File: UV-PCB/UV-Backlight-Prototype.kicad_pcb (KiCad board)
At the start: 2 copper layers, 100 x 100 mm, 67 parts, among them J1 Conn_02x08_Odd_Even

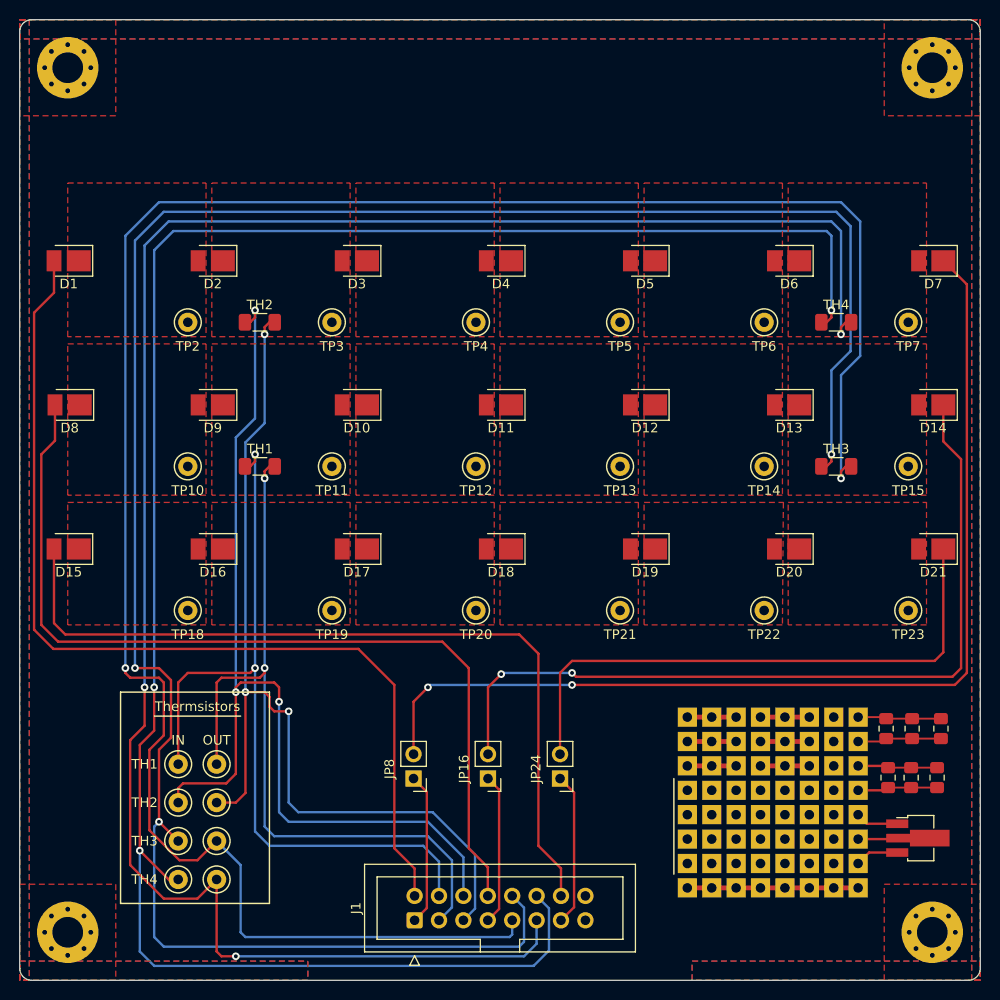
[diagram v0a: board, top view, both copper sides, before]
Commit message: UV Backlight and PS
Power Supply creation
V2 for backlight, removed thermsistors
Changed the connector, simplified the board
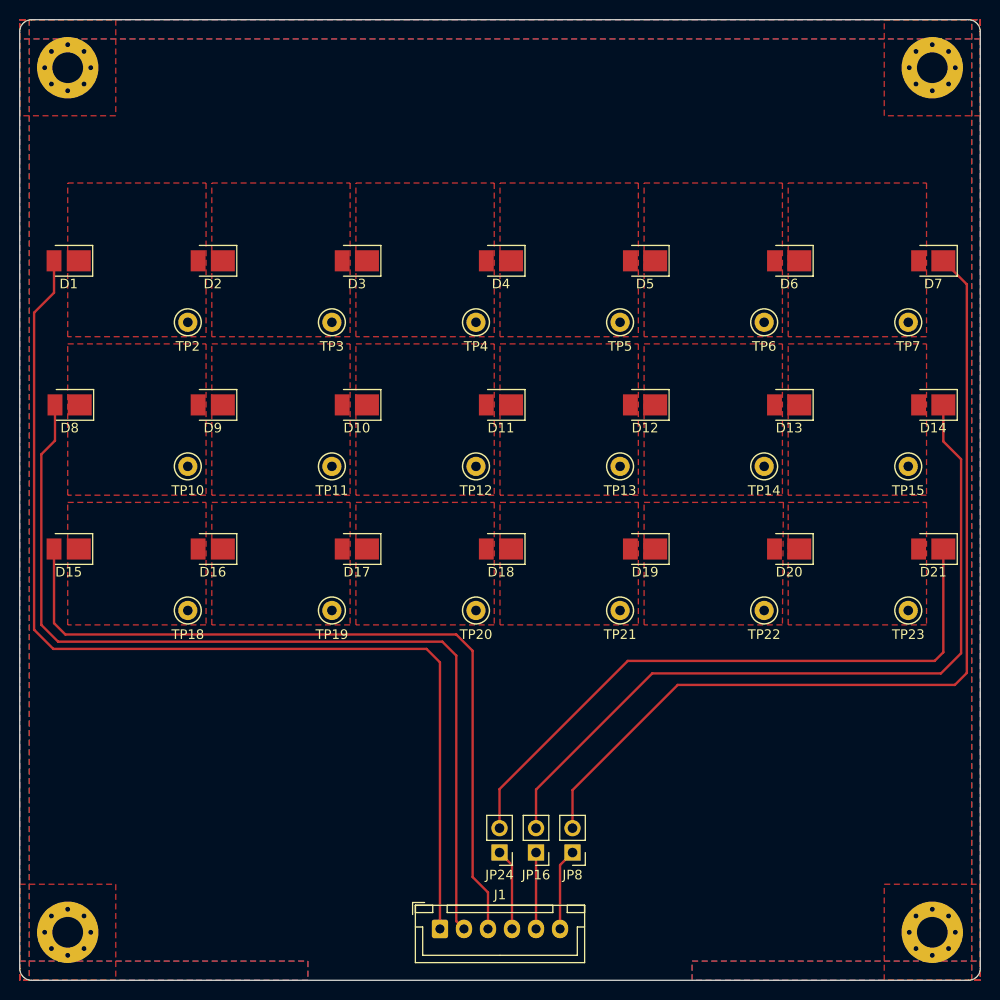
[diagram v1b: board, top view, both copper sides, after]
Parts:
- removed ?: , clipboard:e0d5eb0a-6c50-48e5-8d74-95606411ad53
- removed REF** (x6): C_0805_2012Metric_Pad1.18x1.45mm_HandSolder, Capacitor_SMD:C_0805_2012Metric_Pad1.18x1.45mm_HandSolder
- removed REF**: SOT-89-3_Handsoldering, Package_TO_SOT_SMD:SOT-89-3_Handsoldering
- removed TH1, TH2, TH3, TH4: 10K, Resistor_SMD:R_1206_3216Metric_Pad1.30x1.75mm_HandSolder
- removed TP25: T1-In, TestPoint:TestPoint_Keystone_5000-5004_Miniature
- removed TP26: T1-Out, TestPoint:TestPoint_Keystone_5000-5004_Miniature
- removed TP27: T3-In, TestPoint:TestPoint_Keystone_5000-5004_Miniature
- removed TP28: T3-Out, TestPoint:TestPoint_Keystone_5000-5004_Miniature
- removed TP29: T2-In, TestPoint:TestPoint_Keystone_5000-5004_Miniature
- removed TP30: T2-Out, TestPoint:TestPoint_Keystone_5000-5004_Miniature
- removed TP31: T4-In, TestPoint:TestPoint_Keystone_5000-5004_Miniature
- removed TP32: T4-Out, TestPoint:TestPoint_Keystone_5000-5004_Miniature
- J1: value Conn_02x08_Odd_Even -> Conn_01x06; footprint Connector_IDC:IDC-Header_2x08_P2.54mm_Vertical -> Connector_JST:JST_XH_B6B-XH-A_1x06_P2.50mm_Vertical
- moved JP8 18.3 mm to (157.6, 126.7)
- moved JP24 9.95 mm to (149.9, 126.7)
- moved JP16 9.18 mm to (153.8, 126.7)
- moved J1 2.79 mm to (143.8, 134.7), turned to 0 degrees
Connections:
- J1 pad 1: GND-LED1 -> VCC-LED1
- J1 pad 2: VCC-LED1 -> VCC-LED2
- J1 pad 3: T1-Out -> VCC-LED3
- J1 pad 4: T1-In -> GND-LED3
- J1 pad 5: T2-Out -> GND-LED2
- J1 pad 6: T2-In -> GND-LED1
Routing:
- net T3-In: track 226.4 -> 0.00 mm, vias 3 -> 0
- net T3-Out: track 224.0 -> 0.00 mm, vias 2 -> 0
- net T4-In: track 210.3 -> 0.00 mm, vias 3 -> 0
- net T4-Out: track 207.1 -> 0.00 mm, vias 3 -> 0
- net T2-In: track 102.8 -> 0.00 mm, vias 3 -> 0
- net T2-Out: track 98.4 -> 0.00 mm, vias 3 -> 0
- net (no net): track 95.5 -> 0.00 mm
- net T1-In: track 81.4 -> 0.00 mm, vias 2 -> 0
- net T1-Out: track 80.4 -> 0.00 mm, vias 2 -> 0
- net Net-(D7-Pad1): track 108.2 -> 94.0 mm, vias 2 -> 0
- net VCC-LED1: track 102.0 -> 110.7 mm
- net GND-LED2: track 15.7 -> 7.95 mm
- net GND-LED3: track 15.9 -> 8.49 mm
- net GND-LED1: track 15.9 -> 8.49 mm
- net Net-(D21-Pad1): track 60.0 -> 66.9 mm
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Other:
- board text removed: "IN"
- board text removed: "OUT"
- board text removed: "TH1"
- board text removed: "TH2"
- board text removed: "TH3"
- board text removed: "TH4"
- board text removed: "Thermsistors"
